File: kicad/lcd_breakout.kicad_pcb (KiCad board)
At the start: 2 copper layers, 4 parts, among them J1 Conn_01x05_Male, U1 AY0438X-P, U2 DE119

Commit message: Work on routing
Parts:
- J1: footprint Connector_PinHeader_2.54mm:PinHeader_1x05_P2.54mm_Vertical_SMD_Pin1Right -> Connector_PinHeader_2.54mm:PinHeader_1x05_P2.54mm_Vertical
- moved J1 48.3 mm to (100.6, 110.2), turned to 0 degrees
- moved C1 26.6 mm to (100.6, 104.1), turned to 90 degrees
- moved U2 3.09 mm to (132.8, 81.8)
- moved U1 1.85 mm to (108.7, 122.4)
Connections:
- net VCC renamed VDD
- C1 pad 1: Net-(C1-Pad1) -> GND
- C1 pad 2: GND -> Net-(C1-Pad2)
- U1 pad 31: Net-(C1-Pad1) -> Net-(C1-Pad2)
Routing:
- net Net-(U1-Pad3): track 0.00 -> 145.6 mm
- net Net-(U1-Pad4): track 0.00 -> 128.3 mm
- net Net-(U1-Pad5): track 0.00 -> 126.4 mm
- net Net-(U1-Pad26): track 0.00 -> 112.1 mm, vias 0 -> 1
- net Net-(U1-Pad10): track 0.00 -> 109.5 mm, vias 0 -> 1
- net Net-(U1-Pad25): track 0.00 -> 102.3 mm, vias 0 -> 1
- net Net-(U1-Pad12): track 0.00 -> 99.0 mm, vias 0 -> 1
- net Net-(U1-Pad13): track 0.00 -> 95.8 mm, vias 0 -> 1
- net Net-(U1-Pad6): track 0.00 -> 88.9 mm
- net Net-(U1-Pad29): track 0.00 -> 85.5 mm
- net Net-(U1-Pad20): track 0.00 -> 85.4 mm, vias 0 -> 1
- net Net-(U1-Pad17): track 0.00 -> 84.5 mm, vias 0 -> 1
- net Net-(U1-Pad28): track 0.00 -> 83.9 mm
- net Net-(U1-Pad21): track 0.00 -> 83.1 mm, vias 0 -> 1
- net Net-(U1-Pad39): track 0.00 -> 80.7 mm, vias 0 -> 1
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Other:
- board outline added: 72.1 x 70.1 mm

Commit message: work on pcb layout
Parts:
- moved C1 33.0 mm to (124.0, 127.5), turned to 0 degrees
- moved J1 19.5 mm to (108.7, 128.0), turned to 90 degrees
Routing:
- net GND: track 0.00 -> 59.5 mm, vias 0 -> 1
- net Net-(U1-Pad21): track 83.1 -> 135.5 mm, vias 1 -> 0
- net Net-(U1-Pad3): track 145.6 -> 109.4 mm
- net Net-(C1-Pad2): track 46.3 -> 74.5 mm, vias 0 -> 1
- net Net-(U1-Pad25): track 102.3 -> 127.1 mm
- net Net-(J1-Pad3): track 20.4 -> 41.6 mm, vias 0 -> 1
- net Net-(J1-Pad2): track 26.3 -> 46.7 mm, vias 0 -> 1
- net VDD: track 23.8 -> 5.59 mm
- net Net-(U1-Pad19): track 60.3 -> 44.3 mm, vias 1 -> 0
- net Net-(U1-Pad5): track 126.4 -> 140.2 mm
- net Net-(U1-Pad18): track 80.3 -> 89.1 mm
- net Net-(U1-Pad26): track 112.1 -> 120.7 mm
- net Net-(U1-Pad10): track 109.5 -> 100.9 mm
- net Net-(U1-Pad17): track 84.5 -> 91.1 mm
- net Net-(J1-Pad4): track 14.9 -> 9.59 mm
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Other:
- board size 72.1 x 70.1 mm -> 72.1 x 77 mm

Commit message: pcb clean up for plotting
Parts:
- added REF**: MountingHole_3.5mm, MountingHole:MountingHole_3.5mm, F.Cu at (100.0, 57.0)
- added REF**: MountingHole_3.5mm, MountingHole:MountingHole_3.5mm, F.Cu at (162.0, 57.0)
- added REF**: MountingHole_3.5mm, MountingHole:MountingHole_3.5mm, F.Cu at (100.0, 133.0)
- added REF**: MountingHole_3.5mm, MountingHole:MountingHole_3.5mm, F.Cu at (162.0, 133.0)
- U2: value DE119 -> DE-119
- moved U2 1.27 mm to (131.8, 81.0)
- moved U1 1.27 mm to (107.7, 121.7)
- moved J1 1.27 mm to (107.7, 127.3)
- moved C1 1.27 mm to (122.9, 126.7)
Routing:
- net Net-(J1-Pad3): track 41.6 -> 39.7 mm
- net Net-(J1-Pad2): track 46.7 -> 45.1 mm
- net Net-(U1-Pad5): track 140.2 -> 139.2 mm
- net Net-(U1-Pad3): track 109.4 -> 110.4 mm
- net Net-(U1-Pad4): track 129.6 -> 130.5 mm
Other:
- board size 72.1 x 77 mm -> 74 x 88 mm
- board text added: "LCD Breakout Board"
- board text added: "Tarn Barford"
- board text added: "v1.0"

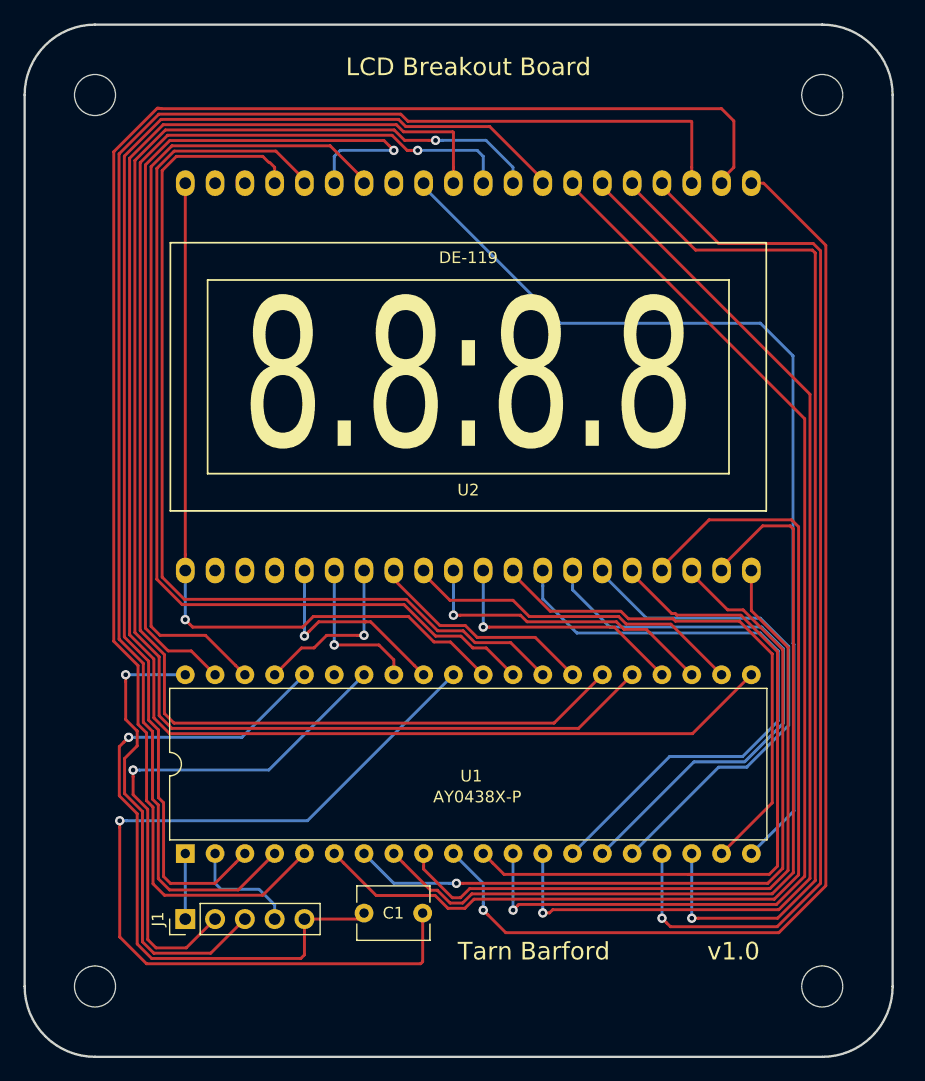
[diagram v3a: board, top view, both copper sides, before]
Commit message: error in schematic fixed
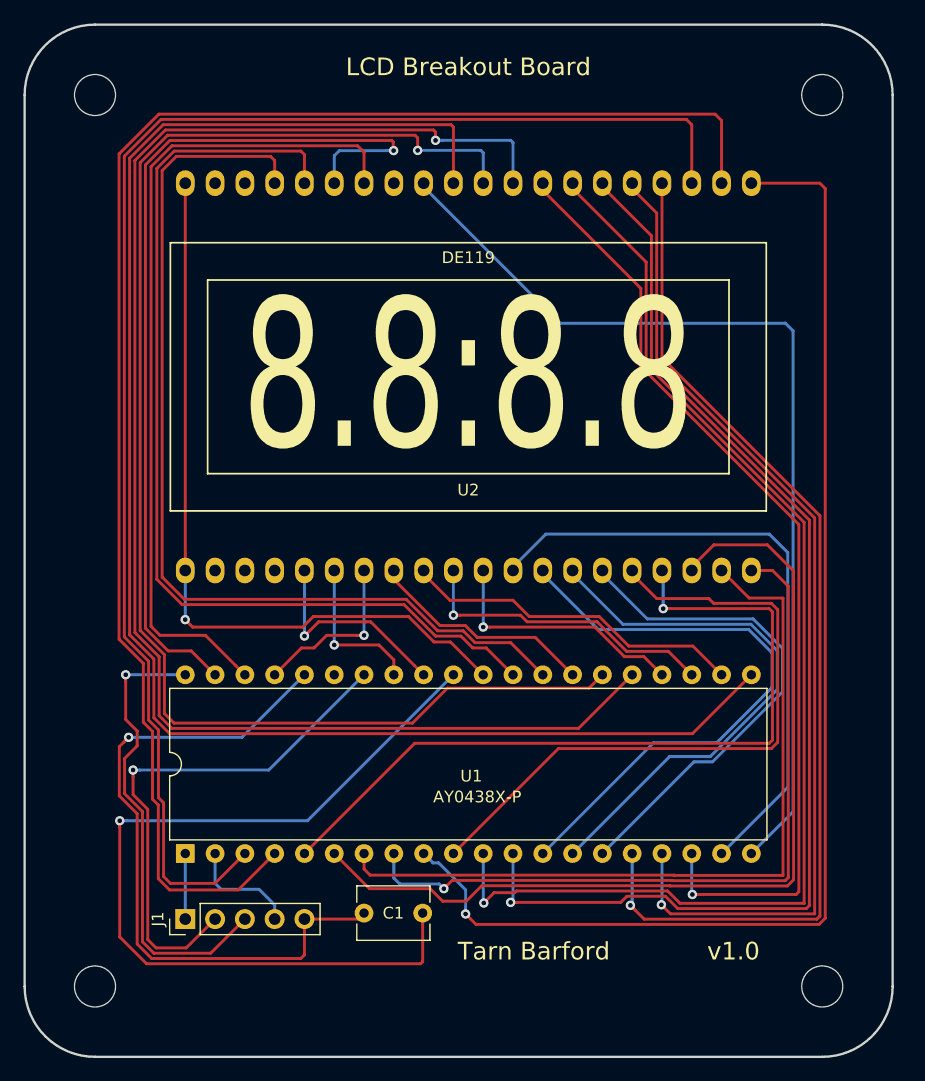
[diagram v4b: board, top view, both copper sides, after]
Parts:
- U2: value DE-119 -> DE119
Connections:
- U2 pad 13: Net-(U1-Pad14) -> Net-(U1-Pad13)
- U2 pad 14: Net-(U1-Pad15) -> Net-(U1-Pad14)
- U2 pad 15: Net-(U1-Pad16) -> Net-(U1-Pad15)
- U2 pad 16: Net-(U1-Pad11) -> Net-(U1-Pad10)
- U2 pad 17: Net-(U1-Pad6) -> Net-(U1-Pad5)
- U2 pad 18: Net-(U1-Pad7) -> Net-(U1-Pad6)
- U2 pad 19: Net-(U1-Pad8) -> Net-(U1-Pad7)
- U2 pad 20: Net-(U1-Pad9) -> Net-(U1-Pad8)
- U2 pad 21: Net-(U1-Pad10) -> Net-(U1-Pad9)
- U2 pad 22: Net-(U1-Pad5) -> Net-(U1-Pad4)
- U2 pad 23: Net-(U1-Pad4) -> Net-(U1-Pad3)
- U2 pad 24: Net-(U1-Pad17) -> Net-(U1-Pad16)
- U2 pad 25: Net-(U1-Pad18) -> Net-(U1-Pad17)
- U2 pad 26: Net-(U1-Pad13) -> Net-(U1-Pad12)
- U2 pad 27: Net-(U1-Pad12) -> Net-(U1-Pad11)
- U2 pad 28: Net-(U1-Pad3) -> Net-(U1-Pad18)
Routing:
- net Net-(U1-Pad5): track 139.2 -> 68.2 mm, vias 0 -> 1
- net Net-(U1-Pad16): track 43.6 -> 89.6 mm, vias 0 -> 1
- net Net-(U1-Pad9): track 61.5 -> 107.1 mm, vias 0 -> 1
- net Net-(U1-Pad13): track 95.7 -> 51.0 mm, vias 1 -> 0
- net Net-(U1-Pad10): track 100.9 -> 56.9 mm, vias 1 -> 0
- net Net-(U1-Pad11): track 60.0 -> 102.3 mm, vias 0 -> 1
- net Net-(U1-Pad3): track 110.4 -> 125.9 mm
- net Net-(U1-Pad19): track 44.3 -> 54.1 mm
- net Net-(U1-Pad8): track 74.2 -> 65.3 mm, vias 0 -> 1
- net Net-(U1-Pad6): track 86.2 -> 78.9 mm
- net Net-(U1-Pad18): track 89.1 -> 82.4 mm
- net Net-(U1-Pad14): track 52.8 -> 47.0 mm
- net Net-(U1-Pad15): track 48.4 -> 43.1 mm
- net Net-(U1-Pad17): track 91.1 -> 86.5 mm
- net Net-(U1-Pad4): track 130.5 -> 133.4 mm
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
